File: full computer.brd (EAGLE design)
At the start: 160 x 95.6 mm, 70 parts, among them IC2 74HC541N, IC3 74HC573N, IC4 74HC04N

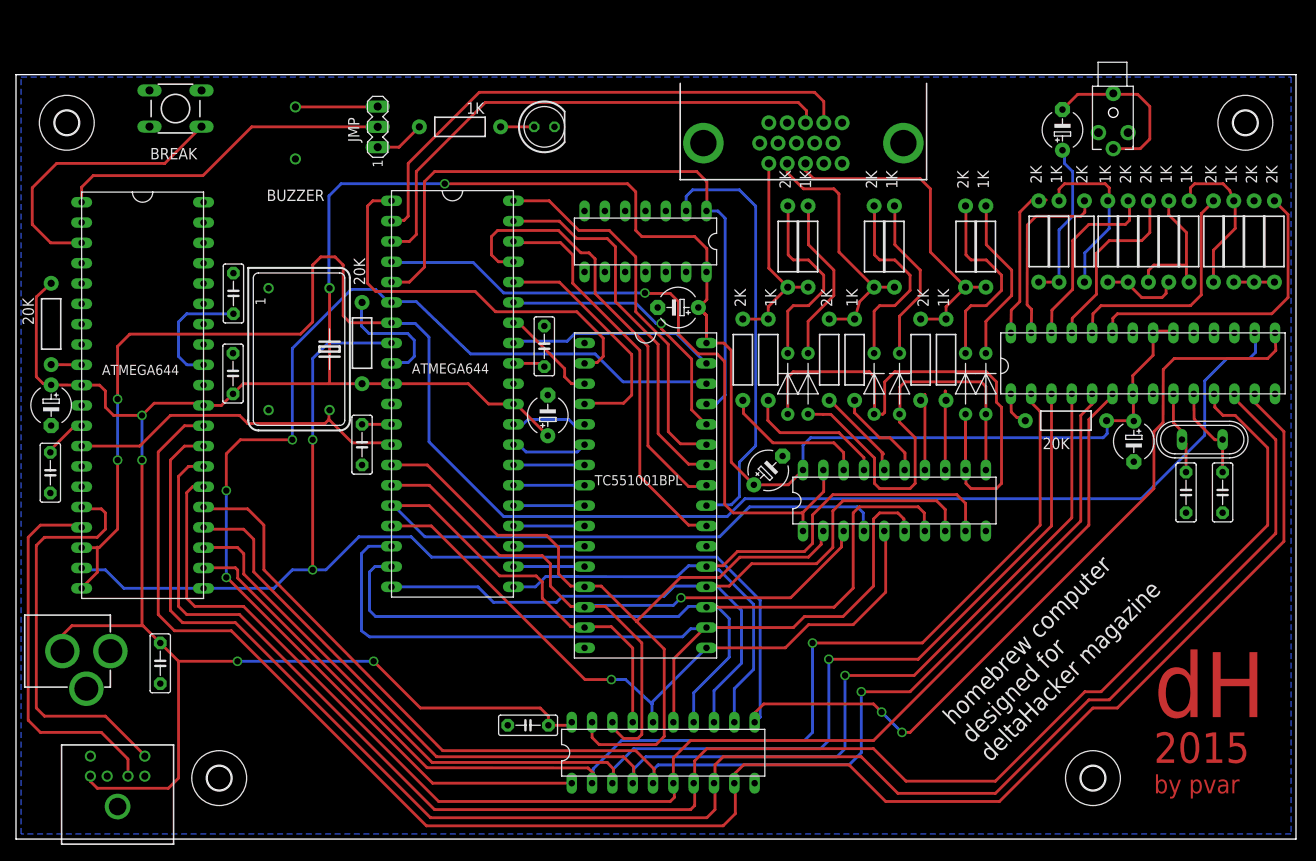
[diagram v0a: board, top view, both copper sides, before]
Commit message: moved PS2 to rear side and BREAK button to front side, the board is now a bit smaller
Signed-off-by: Panagiotis Varelas <varelaspanos@gmail.com>
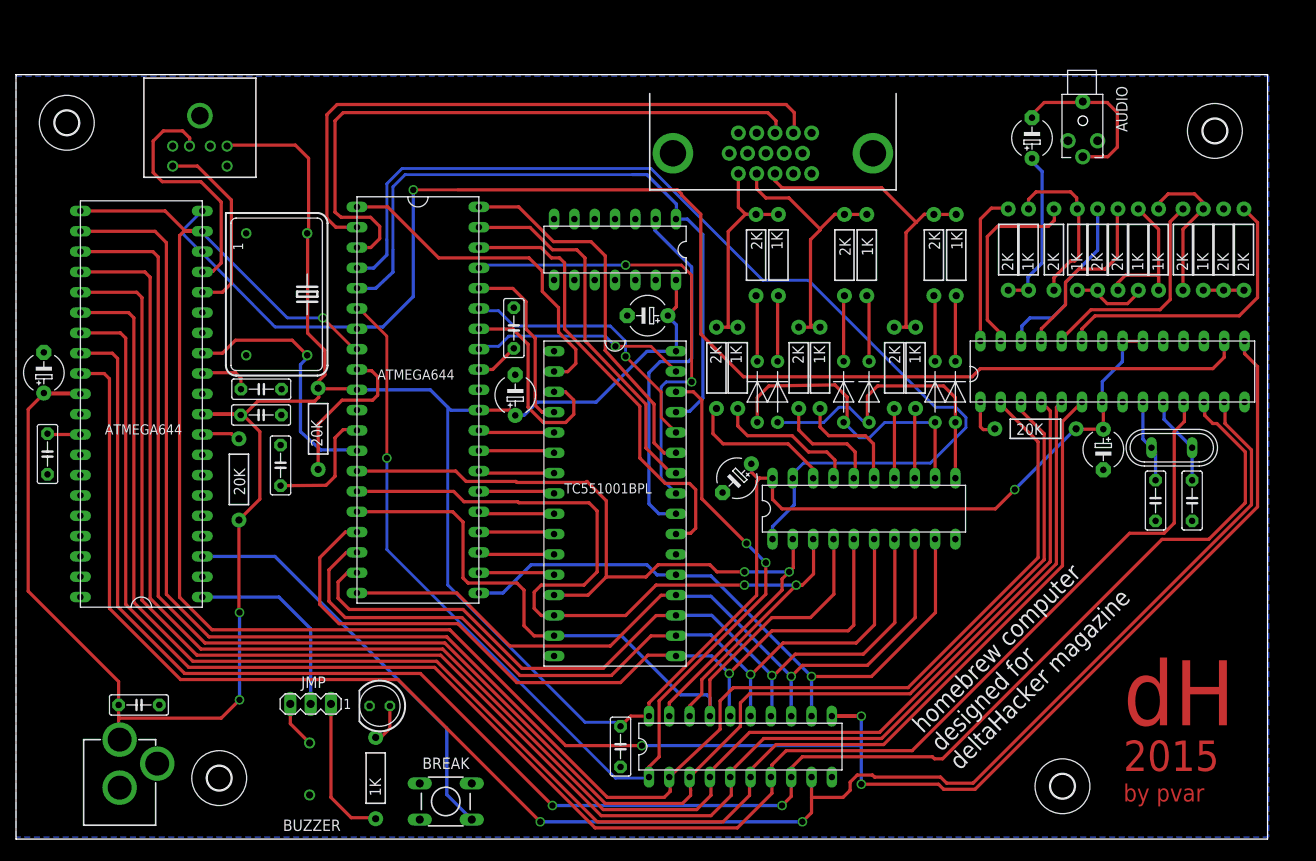
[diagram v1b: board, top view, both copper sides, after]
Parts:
- JP1: value (none) -> AUDIO
- U$39: value MINI-DIN6 -> KEYBOARD
- U$40: value DSUB15 -> MONITOR
- moved U$39 96.3 mm to (23.0, 99.6), turned to 0 degrees
- moved BREAK 93.0 mm to (53.7, 9.14)
- moved U$24 82.1 mm to (45.0, 12.1), turned to 270 degrees
- moved BUZZER 79.5 mm to (36.7, 13.2)
- moved LED1 75.3 mm to (45.5, 21.1), turned to 180 degrees
- moved JMP 72.6 mm to (36.8, 21.3), turned to 180 degrees
- moved C2 30.7 mm to (3.94, 52.6), turned to 270 degrees
- moved U$23 30.5 mm to (27.9, 49.4), turned to 270 degrees
- moved JP2 28.9 mm to (13.0, 3.17), turned to 0 degrees
- moved C10 28.4 mm to (30.7, 60.7), turned to 0 degrees
- moved U$10 12.0 mm to (37.8, 55.7), turned to 90 degrees
- moved C11 11.9 mm to (75.6, 16.0), turned to 270 degrees
- moved C5 10.5 mm to (33.1, 51.2), turned to 90 degrees
- moved IC3 9.68 mm to (90.6, 16.0)
- moved QG1 7.41 mm to (32.6, 72.5)
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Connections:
- net GND: now also JP2.GND, JP2.GNDBREAK; no longer JP2.PWR
- net VCC: now also JP2.PWR; no longer JP2.GND
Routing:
- net CPUDATA0: track 155.0 -> 211.7 mm, vias 1 -> 0
- net CPUDATA1: track 157.7 -> 210.6 mm, vias 1 -> 0
- net TO_CPU: track 225.1 -> 175.6 mm, vias 2 -> 1
- net N$6: track 86.3 -> 134.0 mm, vias 1 -> 0
- net CPUDATA2: track 161.2 -> 207.7 mm, vias 1 -> 0
- net CPUDATA3: track 164.0 -> 206.7 mm, vias 1 -> 0
- net FROM_CPU: track 242.7 -> 285.1 mm
- net N$29: track 74.3 -> 38.9 mm
- net CPUDATA4: track 173.9 -> 206.5 mm
- net PS2_CLOCK: track 51.2 -> 23.6 mm
- net DATA2: track 113.1 -> 94.1 mm
- net DATA1: track 95.2 -> 113.4 mm, vias 1 -> 2
- net N$21: track 42.0 -> 24.6 mm
- net N$22: track 36.0 -> 52.2 mm
- net N$13: track 24.4 -> 8.25 mm
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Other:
- board size 160 x 95.6 mm -> 156.4 x 95.6 mm
- board text added: "AUDIO"

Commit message: added SD card holder & rounded corners
Signed-off-by: Panagiotis Varelas <varelaspanos@gmail.com>
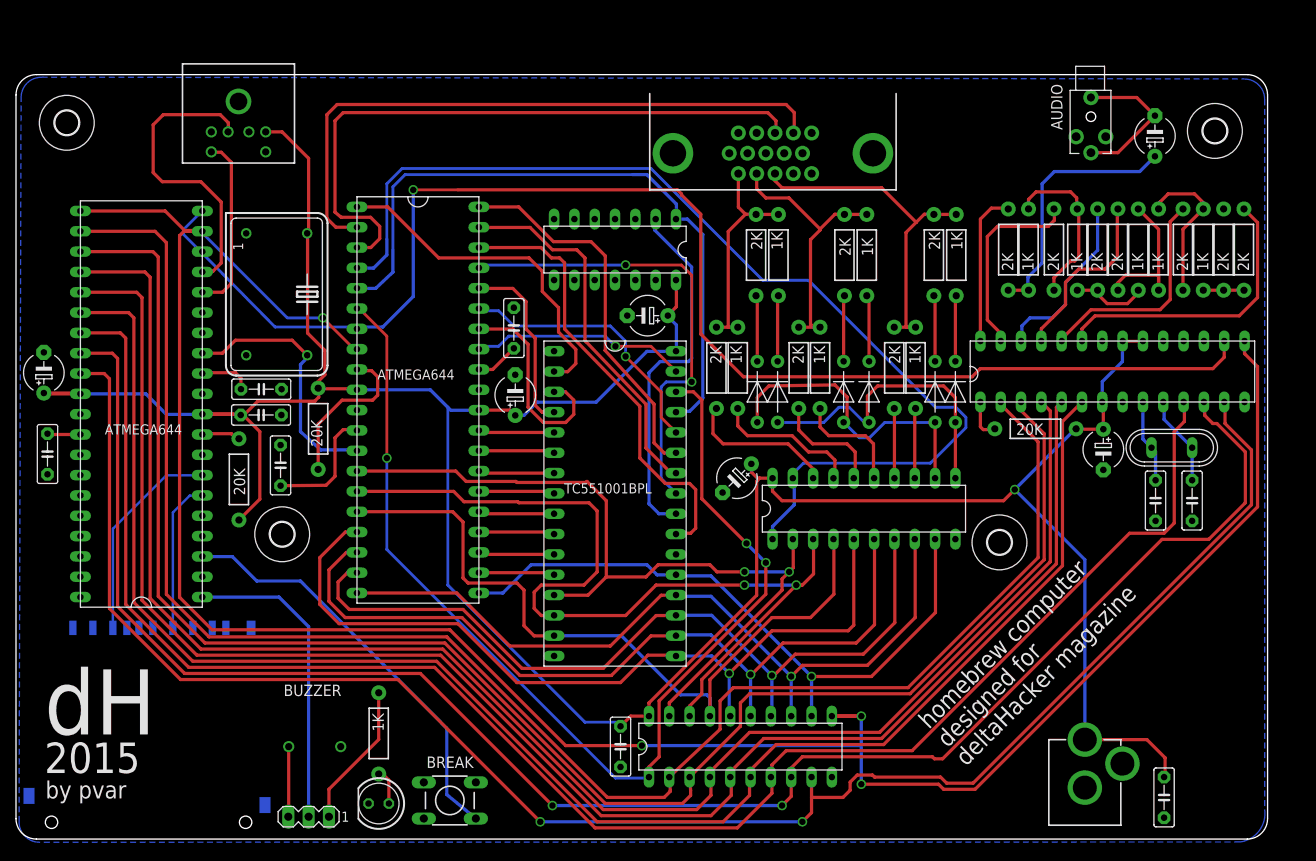
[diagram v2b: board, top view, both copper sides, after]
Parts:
- added U1: SD_CARD_SOCKET4UCON, SparkFun-Connectors:SDCARD_4UCONN
- moved C1 128.7 mm to (143.5, 9.65), turned to 270 degrees
- moved JP2 120.7 mm to (133.6, 3.17)
- moved H4 31.5 mm to (33.3, 42.5)
- moved H5 31.5 mm to (122.9, 41.5)
- moved C13 15.4 mm to (142.4, 92.3)
- moved JMP 14.1 mm to (36.6, 7.24)
- moved LED1 12.2 mm to (45.3, 8.89)
- moved U$24 5.60 mm to (45.3, 17.7), turned to 90 degrees
- moved U$39 5.14 mm to (27.8, 101.3)
- moved BUZZER 2.87 mm to (37.3, 16.0), turned to 180 degrees
- moved JP1 1.14 mm to (134.4, 94.7)
- moved BREAK 0.52 mm to (54.2, 9.27)
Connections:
- new net N$47: U$1.PB5, U1.5
- new net N$48: U$1.PB6, U1.2
- new net VDD: U1.4
- new net VSS1: U1.3
- new net VSS2: U1.6
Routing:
- net VCC: track 392.2 -> 363.6 mm, vias 3 -> 1
- net N$48: track 0.00 -> 26.3 mm
- net N$47: track 0.00 -> 19.0 mm
- net N$21: track 24.6 -> 38.6 mm
- net N$9: track 20.3 -> 32.1 mm
- net PS2_DATA: track 30.9 -> 37.9 mm
- net N$18: track 5.88 -> 8.78 mm
- net AUDIO-OUT: track 21.4 -> 18.9 mm
- net PS2_CLOCK: track 23.6 -> 22.3 mm
- net N$20: track 5.05 -> 4.51 mm
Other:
- outline, holes or cut-outs redrawn

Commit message: removed SD card holder & added external SRAM & reverse voltage protection
Signed-off-by: Panagiotis Varelas <varelaspanos@gmail.com>
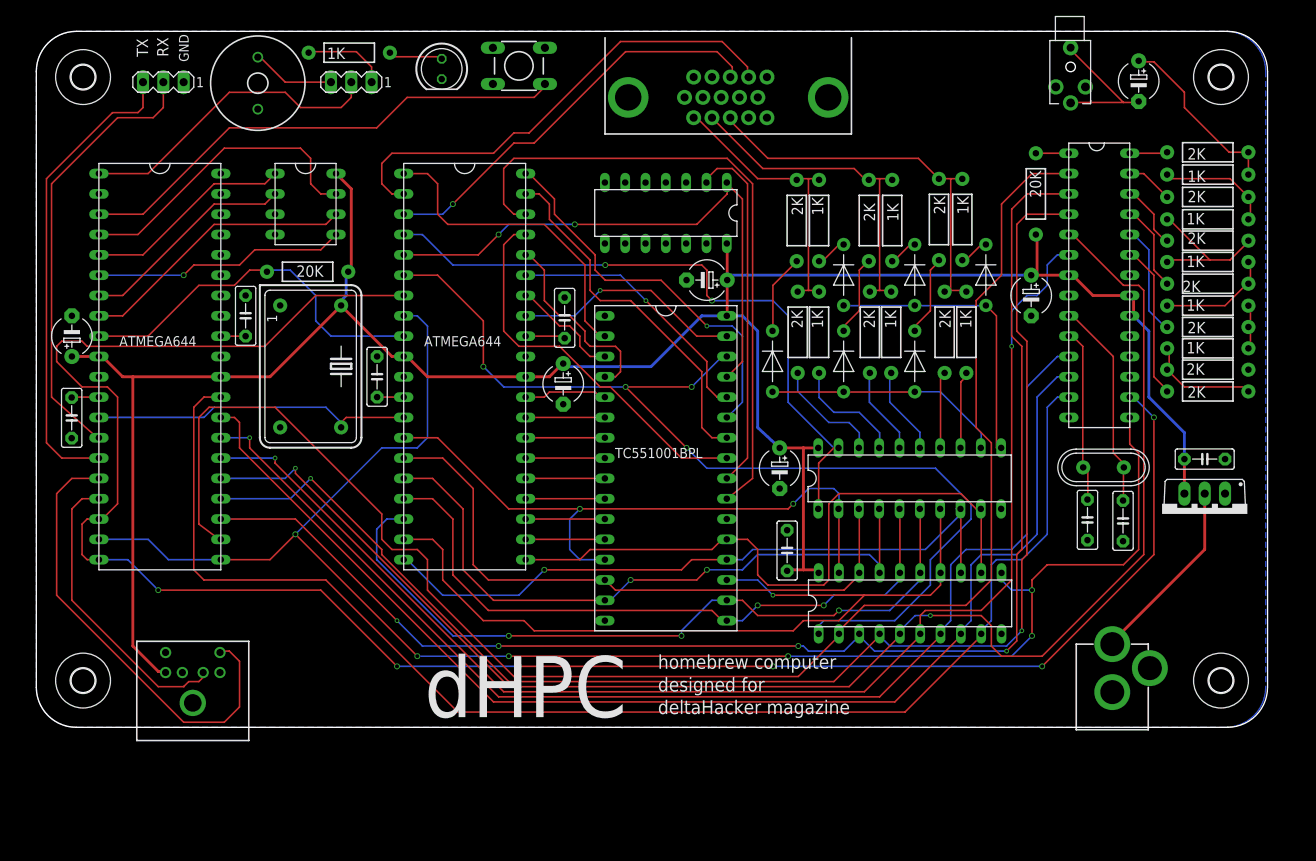
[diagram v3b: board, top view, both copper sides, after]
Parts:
- removed C6: 100nF, capacitor-wima:C5B2.5
- removed U1: SD_CARD_SOCKET4UCON, SparkFun-Connectors:SDCARD_4UCONN
- added JMP1: UART, con-lstb:MA03-1
- added Q1: IRF9530, transistor-power:TO220BV
- U$10: value 20K -> 23LC1024; device SparkFun-Resistors:AXIAL-0.4 -> pvar_parts:23LC1024
- moved H4 118.8 mm to (150.6, 24.3)
- moved H5 115.8 mm to (8.38, 24.3)
- moved BREAK 92.2 mm to (62.9, 101.1)
- moved LED1 92.2 mm to (53.2, 100.7), turned to 270 degrees
- moved JMP 92.0 mm to (41.9, 99.1)
- moved U$24 85.2 mm to (41.7, 102.7), turned to 180 degrees
- moved U$39 84.8 mm to (22.1, 16.8), turned to 180 degrees
- moved BUZZER 83.2 mm to (30.2, 98.9), turned to 90 degrees
- moved C1 42.6 mm to (148.6, 51.9), turned to 0 degrees
- moved C11 32.2 mm to (96.4, 40.5), turned to 90 degrees
- moved C2 30.2 mm to (28.7, 69.8), turned to 90 degrees
- moved U$38 29.4 mm to (127.5, 85.1), turned to 270 degrees
- moved U$10 28.1 mm to (36.2, 83.8), turned to 0 degrees
- moved IC3 27.8 mm to (111.8, 33.9)
- moved U$31 27.8 mm to (149.0, 90.3), turned to 0 degrees
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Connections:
- removed net VDD: U1.4
- removed net VSS1: U1.3
- removed net VSS2: U1.6
- new net N$22: JMP1.2, U$1.PD0
- new net N$50: U$1.PB6, U$10.SO
- new net N$51: U$1.PB5, U$10.SI
- new net N$52: U$1.PB4, U$10.~CS
- new net N$53: U$1.PB3, U$10.~HOLD
- net GND: now also JMP1.1, Q1.G, U$10.VSS; no longer C6.2
- net N$17: now also JP2.PWR, Q1.D; no longer U$1.~RESET, U$23.P$1
- net N$4: now also U$1.~RESET, U$23.P$1; no longer U$10.P$1
- net N$47: now also JMP1.3, U$1.PD1; no longer U$1.PB5, U1.5
- net N$48: now also U$1.PB7, U$10.SCK; no longer U$1.PB6, U1.2
- net VCC: now also Q1.S, U$10.VCC; no longer C6.1, JP2.PWR, U$10.P$2
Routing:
- net FROM_CPU: track 285.1 -> 209.4 mm, vias 4 -> 6
- net VCC: track 363.6 -> 290.9 mm, vias 1 -> 0
- net TO_CPU: track 175.6 -> 247.3 mm, vias 1 -> 6
- net CPUDATA6: track 220.2 -> 154.4 mm, vias 2 -> 0
- net CPUDATA5: track 215.6 -> 153.0 mm, vias 0 -> 1
- net N$22: track 0.00 -> 55.6 mm
- net N$6: track 134.0 -> 82.6 mm, vias 0 -> 2
- net CPUDATA7: track 222.2 -> 171.2 mm, vias 2 -> 0
- net CPUDATA4: track 206.5 -> 163.8 mm, vias 0 -> 2
- net N$47: track 19.0 -> 59.3 mm
- net CPUDATA1: track 210.6 -> 171.4 mm, vias 0 -> 4
- net N$53: track 0.00 -> 38.3 mm
- net PS2_CLOCK: track 22.3 -> 57.8 mm
- net DATA1: track 113.4 -> 78.5 mm, vias 2 -> 0
- net CPUDATA2: track 207.7 -> 174.9 mm, vias 0 -> 2
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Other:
- board size 156.4 x 95.6 mm -> 153.9 x 87 mm
- board text added: "DEC 2015"
- board text added: "GND"
- board text added: "RX"
- board text added: "TX"
- board text added: "by pvar aka spir@l evolut10n"
- board text added: "dHPC"
- board text removed: "2015"
- board text removed: "AUDIO"
- board text removed: "by pvar"
- board text removed: "dH"

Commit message: board completely redesigned!
Signed-off-by: Panagiotis Varelas <varelaspanos@gmail.com>
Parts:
- removed BREAK: TACTILE-SWITCH-PTH, GeekAmmo:TAC-SWITCH-PTH
- removed BUZZER: BUZZERNS, SparkFun-Electromechanical:BUZZER-12MM-NS
- removed C4: 6.8uF, rcl:E5-5
- removed C7: 100nF, capacitor-wima:C5B2.5
- removed JMP: (no value), con-lstb:MA03-1
- removed JP1: AUDIO, SparkFun-Connectors:STEREOJACK2.5MM_STEREOJACK2.5MM
- added C6: 100nF, SparkFun-Capacitors:CAP-PTH-SMALLEZ
- added D1: (no value), SparkFun-LED:LED5MM
- added GPIO: 22-23-2081, con-molex:22-23-2081
- added ISP: (no value), con-ml:ML6
- added S1, S3: 9450-2, switch-misc:9450-2
- added S2: (no value), switch-omron:B3F-31XX
- added SG1: F/TMB, buzzer:F/TMB
- added X1: 1503_08, con-lumberg:1503_08
- C14, C15: device capacitor-wima:C5B2.5 -> SparkFun-Passives:CAP-PTH-SMALLEZ
- C2, C5: device capacitor-wima:C5B2.5 -> SparkFun-Capacitors:CAP-PTH-SMALLEZ
- H1, H2, H4, H5: device holes:3,0 -> holes:3,6
- JP2: value POWER 5V -> 5V
- LED1: device led:LED5MM -> SparkFun-LED:LED5MM
- U$11, U$12, U$13, U$14, U$15, U$16, U$26, U$27, U$28, U$29, U$30, U$31, U$32, U$33, U$34, U$35, U$36, U$37, U$38, U$4, U$5, U$6, U$7, U$8, U$9: device SparkFun-Resistors:AXIAL-0.4 -> SparkFun-Resistors:AXIAL-0.3EZ
- U$23: value 20K -> 220R; device SparkFun-Resistors:AXIAL-0.4 -> SparkFun-Resistors:AXIAL-0.3EZ
- U$24: value 1K -> 180R; device SparkFun-Resistors:AXIAL-0.4 -> SparkFun-Resistors:AXIAL-0.3EZ
- moved C10 106.9 mm to (113.7, 51.1), turned to 90 degrees
- moved U$23 106.1 mm to (132.3, 29.8), turned to 90 degrees
- moved U$24 104.7 mm to (117.5, 30.6), turned to 90 degrees
- moved LED1 101.5 mm to (117.9, 22.5), turned to 0 degrees
- moved JMP1 99.6 mm to (69.1, 13.3)
- moved C1 95.6 mm to (62.9, 94.4), turned to 90 degrees
- moved C12 91.9 mm to (88.0, 24.0), turned to 0 degrees
- moved C2 80.7 mm to (95.5, 24.5), turned to 180 degrees
- moved U$1 79.4 mm to (91.8, 35.6), turned to 270 degrees
- moved U$10 71.5 mm to (69.0, 20.3)
- moved QG1 36.7 mm to (53.8, 31.0), turned to 0 degrees
- moved H5 36.5 mm to (43.6, 14.5)
- moved H1 35.4 mm to (43.6, 96.0)
- moved U$39 33.9 mm to (55.4, 10.4)
- moved Q1 29.3 mm to (125.9, 26.5)
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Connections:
- removed net N$46: C7.1, U$2.AREF
- new net N$54: GPIO.2, U$1.PA6
- new net N$55: GPIO.3, U$1.PA5
- new net N$56: GPIO.4, U$1.PA4
- new net N$57: GPIO.5, U$1.PA3
- new net N$58: GPIO.6, U$1.PA2
- new net N$59: GPIO.7, U$1.PA1
- new net N$60: GPIO.8, U$1.PA0
- new net N$61: ISP.5, U$1.~RESET
- new net N$64: Q1.D, S3.1, S3.4, U$23.P$2
- new net N$69: D1.A, U$23.P$1
- net AUDIO-OUT: now also X1.1, X1.3; no longer JP1.SHIELD, JP1.TIP
- net GND: now also C6.2, D1.K, ISP.6, S2.1, SG1.-, X1.2@1, X1.2@2; no longer BREAK.2, BUZZER.-, C4.-, C7.2, JP1.RING1
- net N$17: now also S3.2, S3.5; no longer Q1.D
- net N$18: now also S1.1, SG1.+; no longer BUZZER.+, JMP.3
- net N$19: now also S1.3; no longer JMP.1
- net N$21: now also S1.2; no longer JMP.2
- net N$4: now also GPIO.1, U$1.PA7; no longer U$1.~RESET, U$2.~RESET, U$23.P$1
- net N$48: now also ISP.3
- net N$49: now also S2.2; no longer BREAK.4
- net N$50: now also ISP.1
- net N$51: now also ISP.4
- net VCC: now also C6.1, ISP.2; no longer C4.+, U$23.P$2
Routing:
- net GND: track 0.00 -> 521.5 mm, vias 0 -> 3
- net TO_CPU: track 247.3 -> 135.0 mm, vias 6 -> 0
- net CPUDATA7: track 171.2 -> 62.3 mm
- net CPUDATA3: track 185.8 -> 83.8 mm, vias 2 -> 0
- net CPUDATA0: track 198.8 -> 100.2 mm
- net CPUDATA6: track 154.4 -> 64.6 mm
- net VCC: track 290.9 -> 378.7 mm, vias 0 -> 5
- net CPUDATA5: track 153.0 -> 66.1 mm, vias 1 -> 0
- net CPUDATA4: track 163.8 -> 79.0 mm, vias 2 -> 0
- net CPUDATA2: track 174.9 -> 90.2 mm, vias 2 -> 0
- net N$52: track 26.2 -> 103.6 mm, vias 0 -> 3
- net CPUDATA1: track 171.4 -> 96.5 mm, vias 4 -> 0
- net FROM_CPU: track 209.4 -> 141.5 mm, vias 6 -> 2
- net N$50: track 27.3 -> 82.7 mm
- net N$8: track 130.1 -> 82.6 mm, vias 4 -> 3
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- added copper zone on layer 1, net GND
- removed copper zone on layer 16, net GND
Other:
- board size 153.9 x 87 mm -> 99.6 x 90.2 mm
- board text added: "1"
- board text added: "100nF"
- board text added: "2"
- board text added: "20MHz"
- board text added: "22pF"
- board text added: "23LC1024"
- board text added: "6.8uF"
- board text added: "8"
- board text added: "APU"
- board text added: "AUDIO"
- board text added: "BREAK"
- board text added: "BUZZER"
- board text added: "CLOCK"
- board text added: "CPU"
- board text added: "DAC"
- board text added: "G"
- board text added: "GPIO"
- board text added: "GPU"
- board text added: "KEYBOARD"
- board text added: "LED/BUZ"
- board text added: "MONITOR"
- board text added: "OFF"
- board text added: "ON"
- board text added: "POWER"
- board text added: "SPK"
- board text added: "SRAM"
- board text added: "SYSTEM"
- board text added: "VIDEO DAC"
- board text added: "VRAM"
- board text added: "by spir@l evolut10n"
- board text removed: "DEC 2015"
- board text removed: "GND"
- board text removed: "by pvar aka spir@l evolut10n"
- board text removed: "homebrew computer designed for deltaHacker magazine"
